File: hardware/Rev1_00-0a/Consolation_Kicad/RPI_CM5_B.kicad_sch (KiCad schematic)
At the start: 12 parts, among them J12 RPI_CMx_B, J18 61300411121

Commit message: Continue preliminary placement To do : Power supplies + Type C charger
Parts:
- J18: now not fitted
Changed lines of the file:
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@@
 	(title_block
 		(title "Consolation [Console Emulation]")
-		(date "2026-08-23")
+		(date "2026-08-29")
 		(rev "1.00-0A")
 		(comment 1 "Jean-Francois Bilodeau")
@@
 	)
 	(label "USB_PROG_N"
-		(at 65.405 26.035 0)
+		(at 74.93 26.035 0)
 		(effects
 			(font
@@
 		)
 		(property "Net Class" "DP_90R"
-			(at 94.869 25.146 0)
+			(at 104.394 25.146 0)
 			(show_name no)
 			(do_not_autoplace no)
@@
 	)
 	(label "USB_PROG_P"
-		(at 65.405 28.575 0)
+		(at 74.93 28.575 0)
 		(effects
 			(font
@@
 		)
 		(property "Net Class" "DP_90R"
-			(at 94.869 27.432 0)
+			(at 104.394 27.432 0)
 			(show_name no)
 			(do_not_autoplace no)
@@
 	)
 	(label "USB_PROG_OTG_ID"
-		(at 65.405 23.495 0)
+		(at 74.93 23.495 0)
 		(effects
 			(font
@@
 		(on_board yes)
 		(in_pos_files yes)
-		(dnp no)
+		(dnp yes)
 		(property "Reference" "J18"
 			(at 21.844 21.082 0)

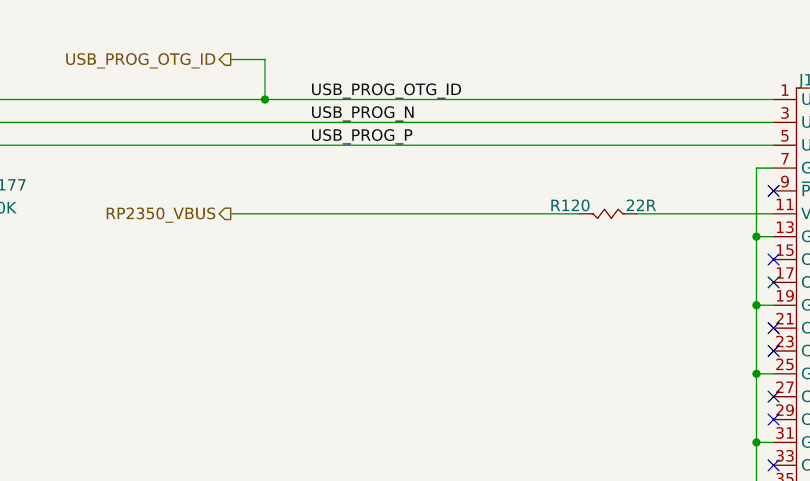
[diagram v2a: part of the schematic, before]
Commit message: Preliminary placement done Add test points to PCB
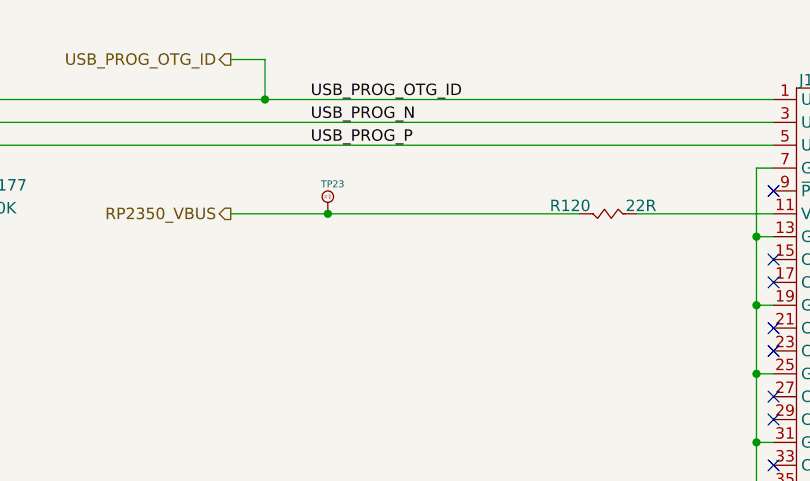
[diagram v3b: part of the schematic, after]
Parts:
- added TP23: 75 mils, footprint:SMT_TP_75_MILS, symbol KicadCompDb:Test Point/TP_00004
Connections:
- net RP2350_VBUS: now also TP23.1
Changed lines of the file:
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@@
 	(title_block
 		(title "Consolation [Console Emulation]")
-		(date "2026-08-29")
+		(date "2026-09-20")
 		(rev "1.00-0A")
 		(comment 1 "Jean-Francois Bilodeau")
@@
 	)
 	(junction
+		(at 76.835 36.195)
+		(diameter 0)
+		(color 0 0 0 0)
+	)
+	(junction
 		(at 124.46 99.695)
 		(diameter 0)
@@
 	(wire
 		(pts
+			(xy 76.835 36.195) (xy 104.775 36.195)
+		)
+		(stroke
+			(width 0)
+			(type default)
+		)
+	)
+	(wire
+		(pts
 			(xy 23.495 28.575) (xy 126.365 28.575)
 		)
@@
 	(wire
 		(pts
-			(xy 66.04 36.195) (xy 104.775 36.195)
+			(xy 66.04 36.195) (xy 76.835 36.195)
 		)
 		(stroke
@@
 					(unit 1)
 				)
+			)
+		)
+	)
+	(symbol
+		(lib_id "KicadCompDb:Test Point/TP_00004")
+		(at 76.835 34.925 90)
+		(unit 1)
+		(body_style 1)
+		(exclude_from_sim no)
+		(in_bom yes)
+		(on_board yes)
+		(in_pos_files yes)
+		(dnp no)
+		(property "Reference" "TP23"
+			(at 76.073 32.893 90)
+			(show_name no)
+			(do_not_autoplace no)
+			(effects
+				(font
+					(size 0.762 0.762)
+				)
+				(justify right)
+			)
+		)
+		(property "Value" "75 mils"
+			(at 77.851 34.29 0)
+			(hide yes)
+			(show_name no)
+			(do_not_autoplace no)
+			(effects
+				(font
+					(size 0.762 0.762)
+				)
+			)
+		)
+		(property "Footprint" "footprint:SMT_TP_75_MILS"
+			(at 78.74 34.925 0)
+			(hide yes)
+			(show_name no)
+			(do_not_autoplace no)
+			(effects
+				(font
+					(size 1.27 1.27)
+				)
+			)
+		)
+		(property "Datasheet" "NA"
+			(at 76.835 34.925 0)
+			(hide yes)
+			(show_name no)
+			(do_not_autoplace no)
+			(effects
+				(font
+					(size 1.27 1.27)
+				)
+			)
+		)
+		(property "Description" "SMT TP 75 mils"
+			(at 76.835 34.925 0)
+			(hide yes)
+			(show_name no)
+			(do_not_autoplace no)
+			(effects
+				(font
+					(size 1.27 1.27)
+				)
+			)
+		)
+		(property "Dimensions" "75 mils"
+			(at 76.835 34.925 0)
+			(hide yes)
+			(show_name yes)
+			(do_not_autoplace no)
+			(effects
+				(font
+					(size 1.27 1.27)
+				)
+			)
+		)
+		(property "Distributor" "NA"
+			(at 76.835 34.925 0)
+			(hide yes)
+			(show_name yes)
+			(do_not_autoplace no)
+			(effects
+				(font
+					(size 1.27 1.27)
+				)
+			)
+		)
+		(property "Distributor Part Number" "NA"
+			(at 76.835 34.925 0)
+			(hide yes)
+			(show_name yes)
+			(do_not_autoplace no)
+			(effects
+				(font
+					(size 1.27 1.27)
+				)
+			)
+		)
+		(property "Manufacturer" "NA"
+			(at 76.835 34.925 0)
+			(hide yes)
+			(show_name yes)
+			(do_not_autoplace no)
+			(effects
+				(font
+					(size 1.27 1.27)
+				)
+			)
+		)
+		(property "Manufacturer Part Number" "NA"
+			(at 76.835 34.925 0)
+			(hide yes)
+			(show_name yes)
+			(do_not_autoplace no)
+			(effects
+				(font
+					(size 1.27 1.27)
+				)
+			)
+		)
+		(property "Operating Temperature" "NA"
+			(at 76.835 34.925 0)
+			(hide yes)
+			(show_name yes)
+			(do_not_autoplace no)
+			(effects
+				(font
+					(size 1.27 1.27)
+				)
+			)
+		)
+		(property "Package" "NA"
+			(at 76.835 34.925 0)
+			(hide yes)
+			(show_name yes)
+			(do_not_autoplace no)
+			(effects
+				(font
+					(size 1.27 1.27)
+				)
+			)
+		)
+		(property "Type" "SMT"
+			(at 76.835 34.925 0)
+			(hide yes)
+			(show_name yes)
+			(do_not_autoplace no)
+			(effects
+				(font
+					(size 1.27 1.27)
+				)
+			)
+		)
+		(pin "1"
+		)
+		(instances
+			(project "Consolation_Kicad"
+				(path "/b18b5a64-cfe0-4447-acaf-556f3c6e6513/e349e81f-8577-4688-9d24-3b63a58130fe"
+					(reference "TP23")
+					(unit 1)
+				)

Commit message: Add preliminary manufacturing files for Consolation Review pinout & design notes
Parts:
- ITEM1: now not fitted
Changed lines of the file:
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@@
 	(title_block
 		(title "Consolation [Console Emulation]")
-		(date "2026-10-27")
+		(date "2026-10-31")
 		(rev "1.00-0A")
 		(comment 1 "Jean-Francois Bilodeau")
@@
 		(on_board yes)
 		(in_pos_files yes)
-		(dnp no)
+		(dnp yes)
 		(property "Reference" "ITEM1"
 			(at 272.669 151.257 0)
